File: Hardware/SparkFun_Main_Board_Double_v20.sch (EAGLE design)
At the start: 88 parts, among them J1 MICROMOD-2222-C, J10 MICRO-SD-PUSH-PUSH-EXT-PIN, J2 Vertical Qwiic Connector, J4 QWIIC_RIGHT_ANGLE, J5 CORTEX_JTAG_DEBUG_MINIMUM_PTH, J6 MICROMOD_FUNCTION_MAIN, J7 MICROMOD_FUNCTION_MAIN, Q1 3.1A/30V/105mΩ, Q2 20V/4.2A/52mΩ/1.4W, U1 STG3856QTR, U2 MCP73831, U3 ESD Diode, U4 AP7347DQ-33W5-7K-3.3V, U5 AP7361C-33

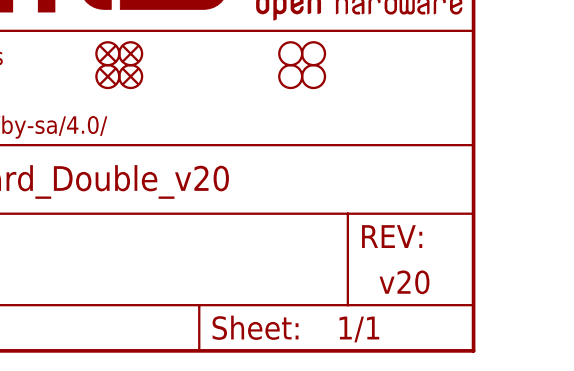
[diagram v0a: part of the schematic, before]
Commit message: Moves I2C pullups to make space for silk
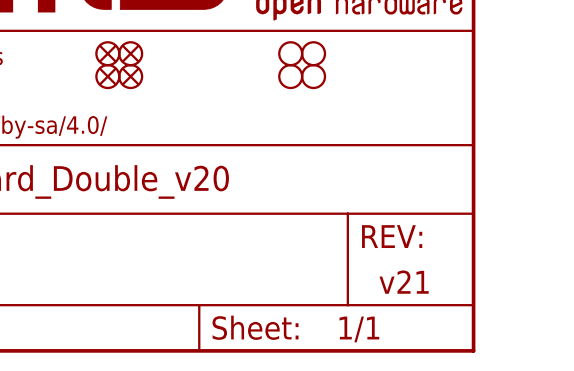
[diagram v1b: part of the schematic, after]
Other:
- note added: "v21"
- note removed: "v20"
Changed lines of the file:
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@@
 <text x="96.774" y="123.952" size="2.54" layer="94" font="vector" align="center">Function Board Connectors</text>
 <text x="95.25" y="271.526" size="2.54" layer="94" font="vector" align="center">Processor Board Connector</text>
-<text x="424.18" y="7.62" size="2.54" layer="94" font="vector" align="center">v20</text>
+<text x="424.18" y="7.62" size="2.54" layer="94" font="vector" align="center">v21</text>
 <wire x1="365.76" y1="132.08" x2="330.2" y2="132.08" width="0.2032" layer="97" style="longdash"/>
 <wire x1="330.2" y1="132.08" x2="287.02" y2="132.08" width="0.2032" layer="97" style="longdash"/>
